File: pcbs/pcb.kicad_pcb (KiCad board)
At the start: 2 copper layers, 152.3 x 118 mm, 97 parts

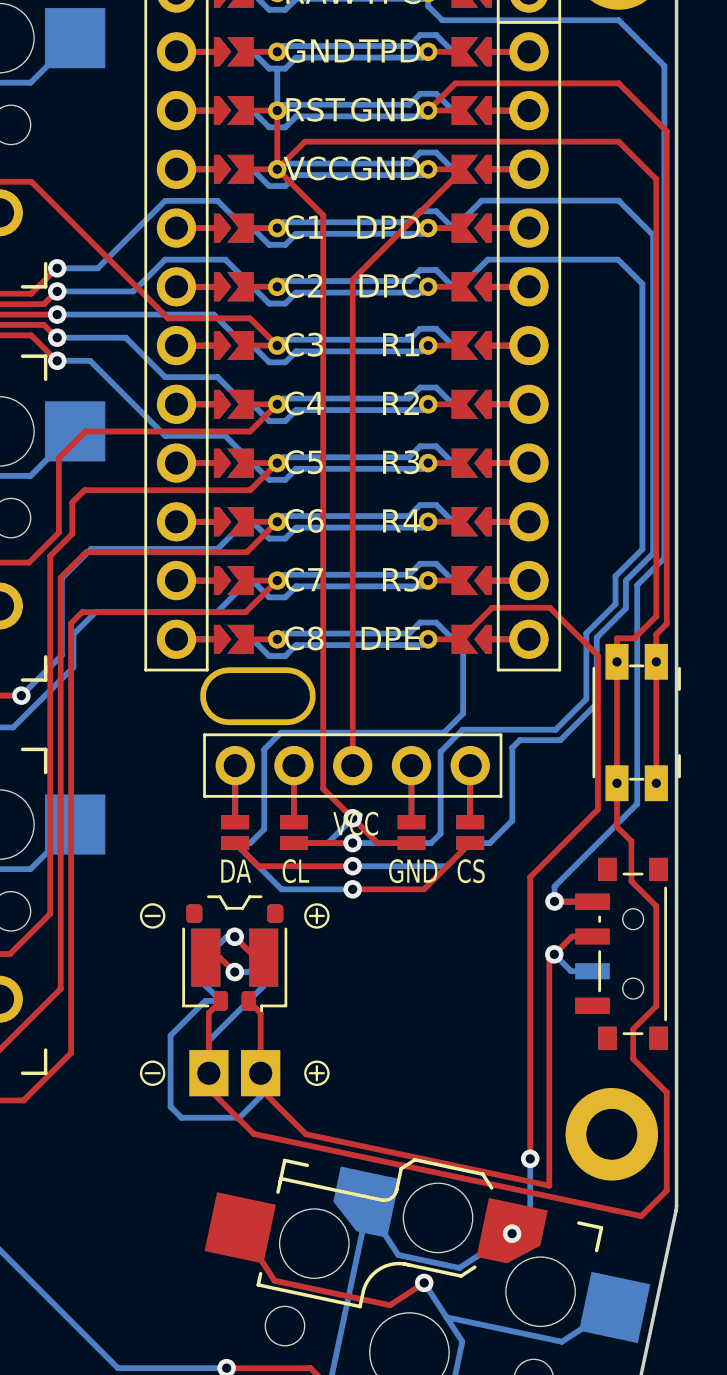
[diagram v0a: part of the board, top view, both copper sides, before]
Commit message: added display cover mount holes and reorganized around to fit
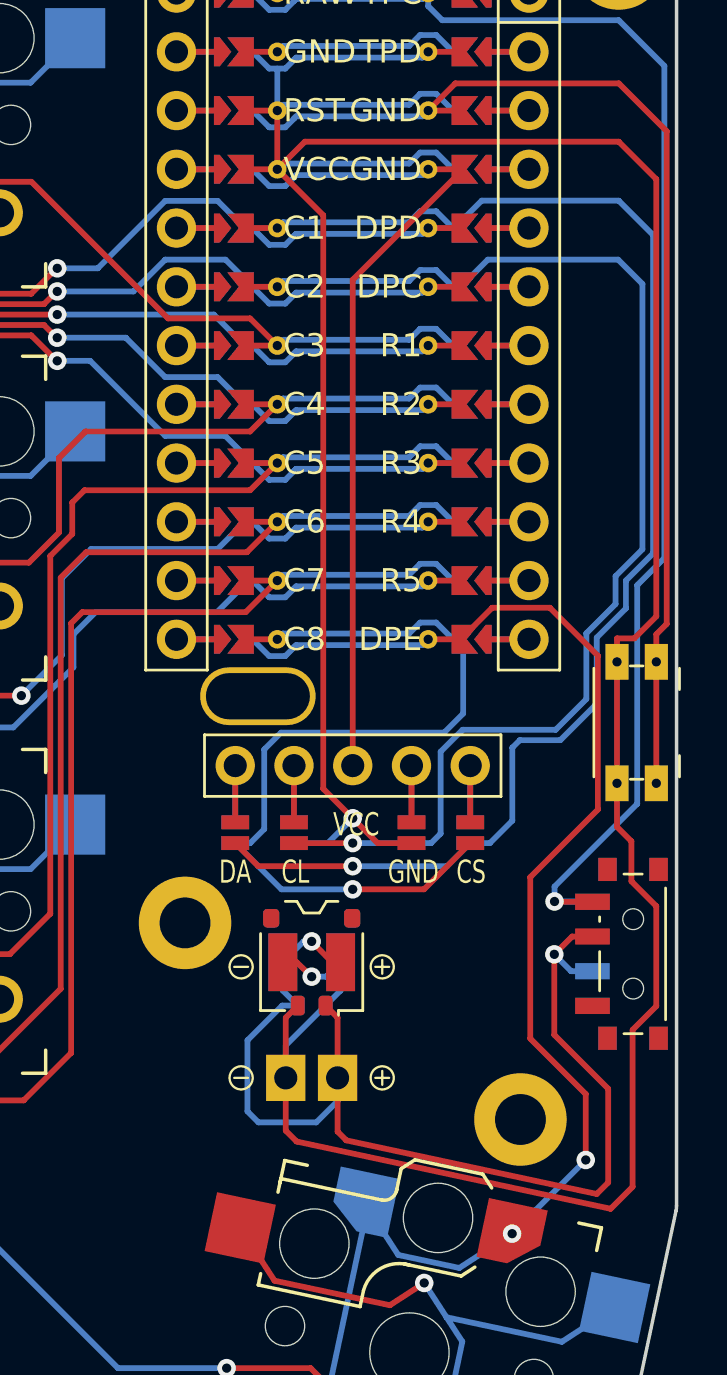
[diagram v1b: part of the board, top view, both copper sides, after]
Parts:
- added H12: , mounting_hole, F.Cu at (235.5, 171.0)
- moved H10 48.0 mm to (224.2, 152.7), turned to 0 degrees
- moved H9 36.1 mm to (217.5, 200.2), turned to -12 degrees
- moved H11 10.3 mm to (221.0, 162.5)
- moved ICON1 3.99 mm to (226.5, 164.4)
- moved ? 3.33 mm to (226.5, 169.2)
- moved CONN1 3.33 mm to (226.5, 164.2)
- moved ICON2 3.33 mm to (226.5, 169.2)
- moved PAD1 3.33 mm to (226.5, 164.2)
- moved PAD2 3.33 mm to (226.5, 169.2)
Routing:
- net (no net): track 5022.0 -> 5020.5 mm

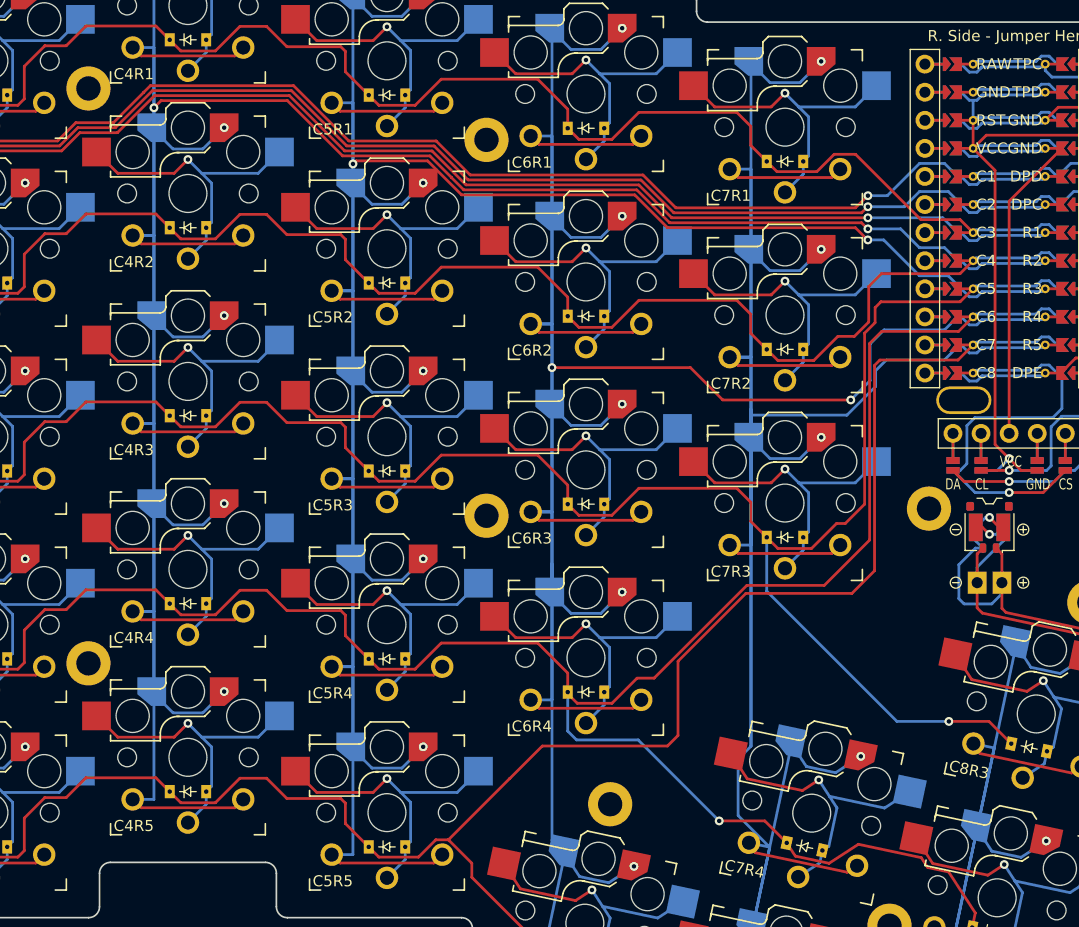
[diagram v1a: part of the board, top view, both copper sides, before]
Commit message: some routing improvements and mounting holes adjustments
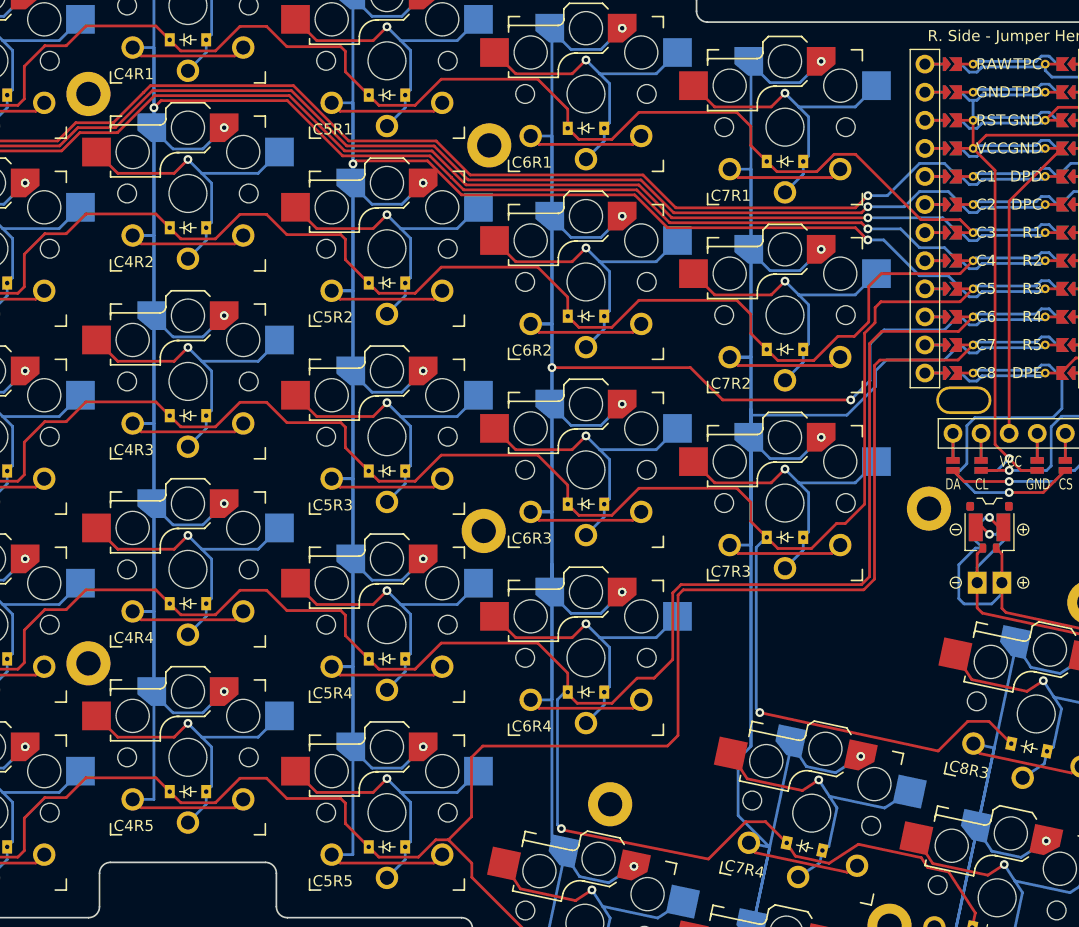
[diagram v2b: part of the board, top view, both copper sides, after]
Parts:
- moved H6 1.40 mm to (180.8, 164.5)
- moved H5 0.56 mm to (181.2, 129.7)
- moved H3 0.50 mm to (145.0, 125.0)
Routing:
- net (no net): track 5020.5 -> 5050.1 mm
